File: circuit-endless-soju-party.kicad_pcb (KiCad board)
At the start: 2 copper layers, 30 x 57.5 mm, 13 parts, among them J1 CAN, J2 UART, SW1 RESET, U1 ESP32-C3-MINI-1-N4, U2 ATA6561-GAQW, U4 AP130-33Y

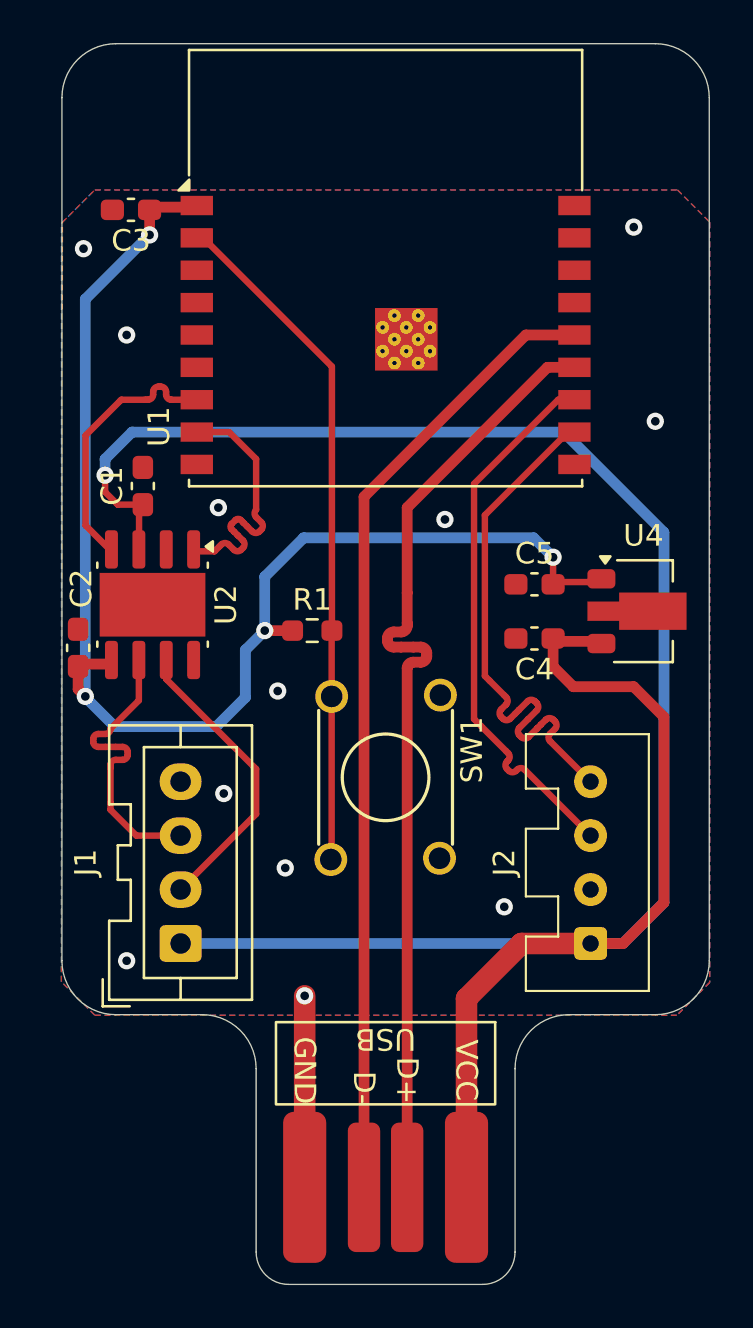
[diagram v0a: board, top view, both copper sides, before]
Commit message: feature: 固定穴を追加。
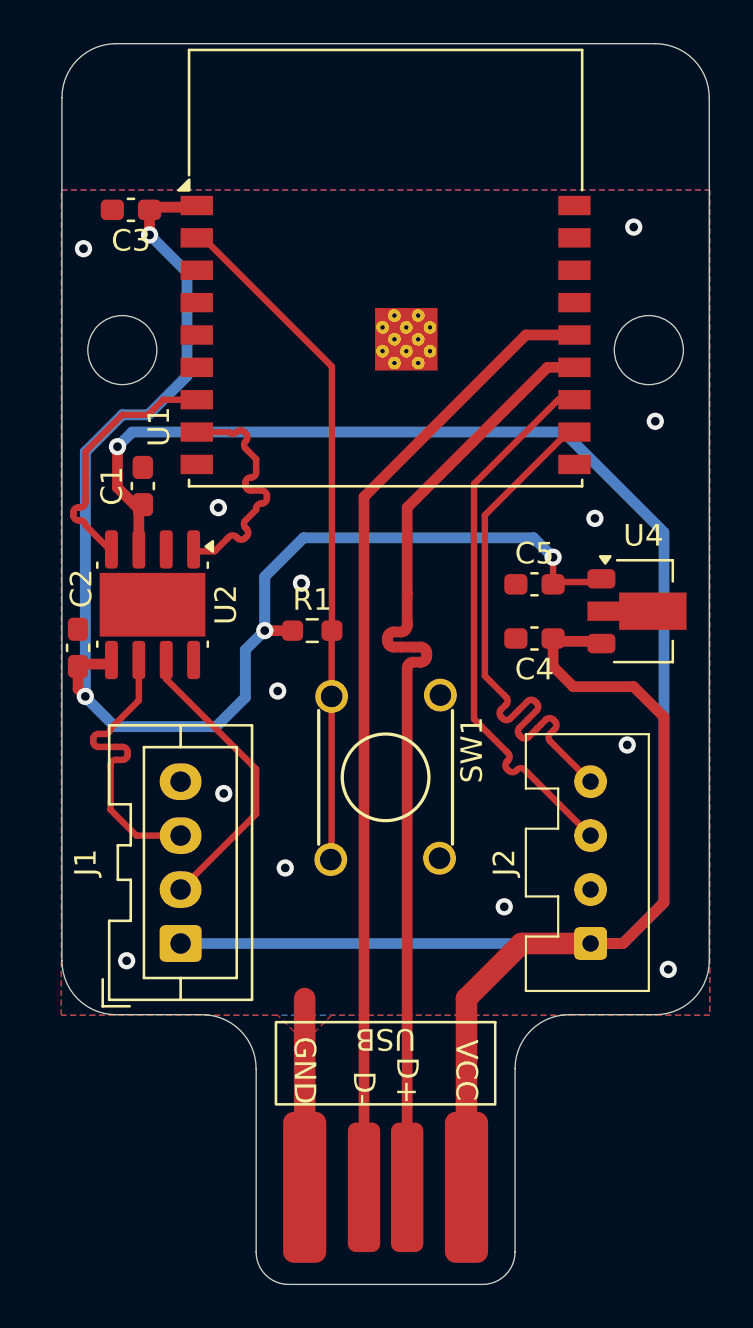
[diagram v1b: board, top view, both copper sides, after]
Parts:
- added  : holeφ3.2, circuit-endless-soju-party:holeφ3.2, F.Cu at (140.2, 70.2)
- added  : holeφ3.2, circuit-endless-soju-party:holeφ3.2, F.Cu at (115.8, 70.2)
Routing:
- net +3.3V: track 63.2 -> 65.3 mm
- net +5V: track 112.4 -> 111.5 mm
- net Net-(U1-IO9/CAN_RX): track 12.4 -> 11.9 mm
- net GND: track 8.88 -> 8.75 mm, vias 12 -> 13

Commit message: feature: GNDのベタ塗りを調整。
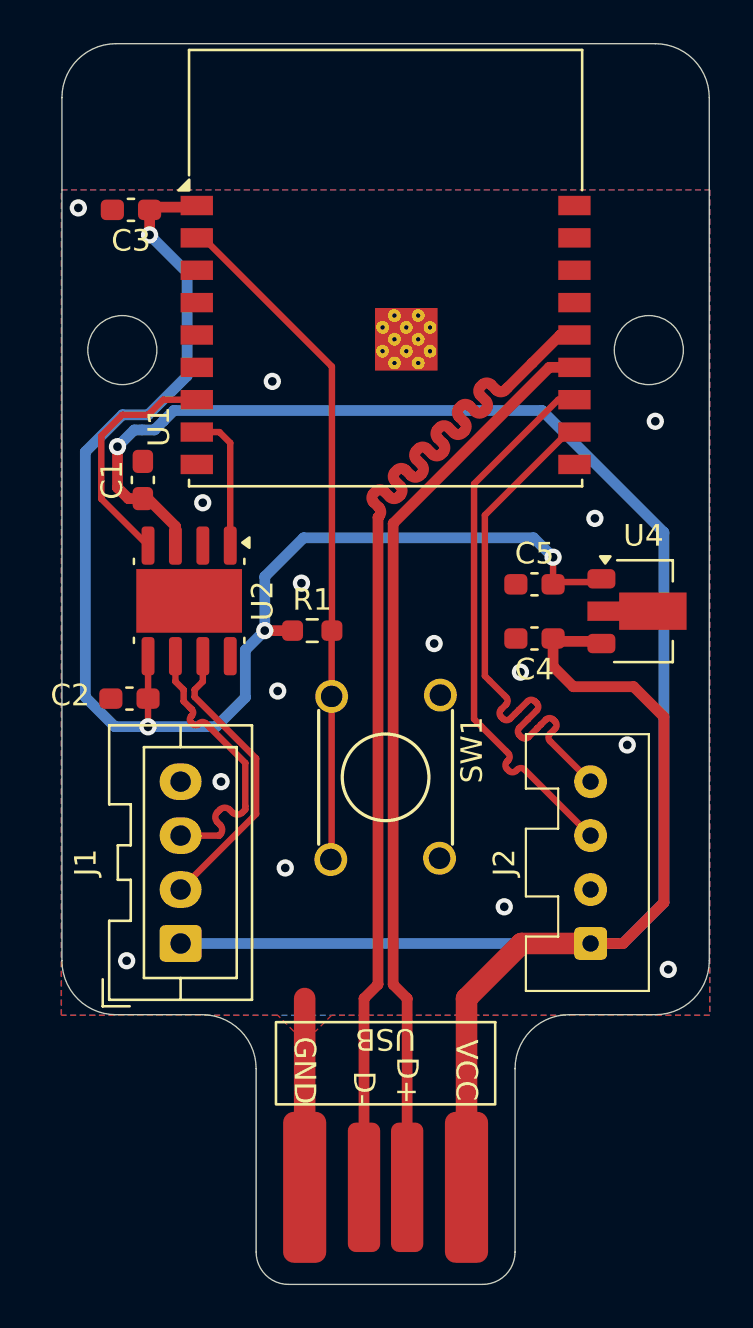
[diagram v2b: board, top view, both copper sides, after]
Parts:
- moved C2 3.34 mm to (116.1, 86.3), turned to 180 degrees
- moved U2 1.70 mm to (118.9, 81.8)
- moved C1 0.28 mm to (116.8, 76.2)
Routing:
- net USB_N: track 44.9 -> 51.8 mm
- net Net-(U1-IO9/CAN_RX): track 11.9 -> 6.52 mm
- net USB_P: track 44.8 -> 42.4 mm
- net +5V: track 111.5 -> 113.0 mm
- net Net-(U1-IO8/CAN_TX): track 12.0 -> 11.1 mm
- net GND: vias 13 -> 15

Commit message: feature: 基板外周にビアを追加。
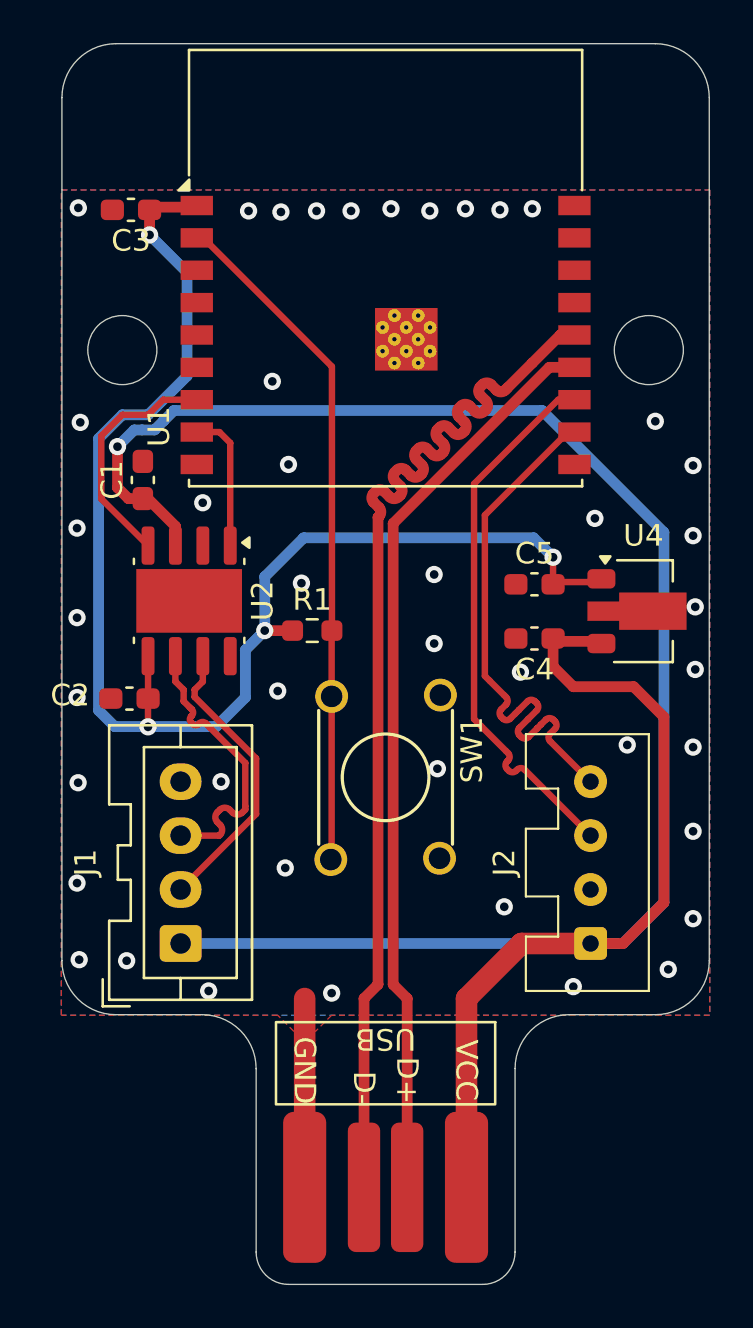
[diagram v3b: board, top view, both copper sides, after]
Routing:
- net +3.3V: track 65.4 -> 64.9 mm
- net GND: vias 15 -> 44

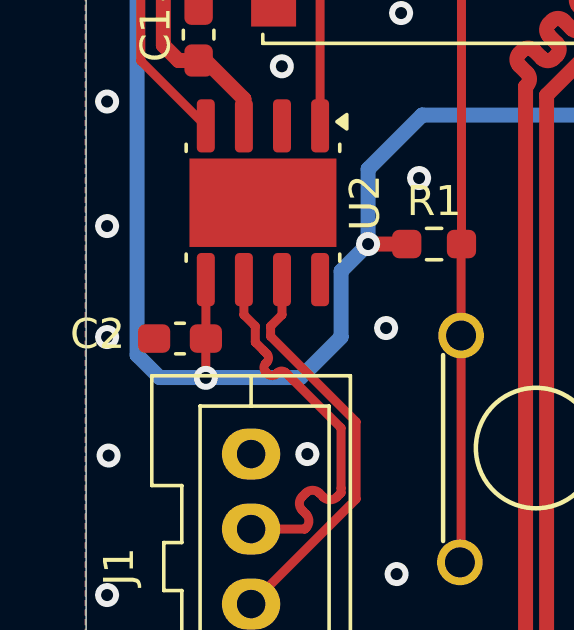
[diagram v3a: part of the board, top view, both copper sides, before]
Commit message: feature: MCUをESP32-C3-MINI-1-N4からESP32-C3-WROOM-02へ変更。
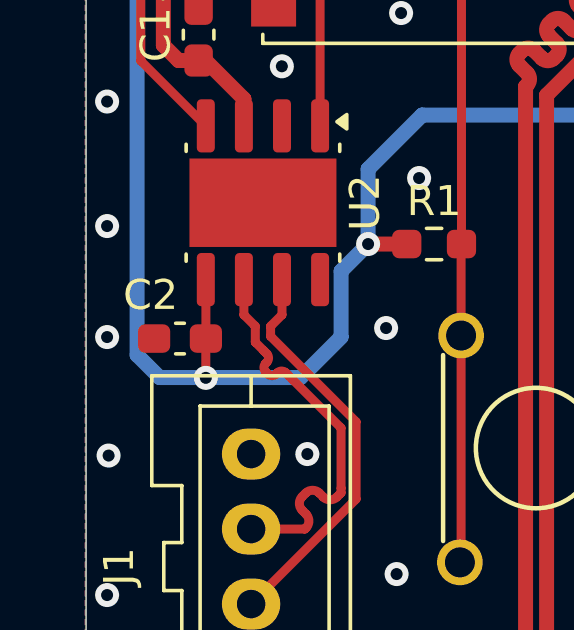
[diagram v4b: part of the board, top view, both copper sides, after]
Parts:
- U1: value ESP32-C3-MINI-1-N4 -> ESP32-C3-WROOM-02

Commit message: feature: ロゴ・リポジトリURLを追加。
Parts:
- added G***: LOGO, circuit-endless-soju-party:LOGO, B.Cu at (127.2, 82.6)
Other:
- board text added: "https://github.com/ mecha-natori/ circuit-endless- soju-party"
- board text added: "終わりなき 操縦 舞踏会"

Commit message: feature: クレジット表記を追加。
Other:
- board text added: "Designed by @ms0503_"
